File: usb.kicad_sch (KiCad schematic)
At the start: 4 parts, among them J3 USB_C_Receptacle_USB2.0_16P, U4 CP2102N-Axx-xQFN20, U5 USBLC6-2SC6

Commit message: did power and usb
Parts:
- added R10, R8, R9: 10k, symbol Device:R
- added R11, R12: 5.1k, Resistor_SMD:R_0402_1005Metric, symbol Device:R
- added R7: 4.7k, symbol Device:R
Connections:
- net SUSPb: now reaches U4.11 (~{SUSPEND})
- net SUSPb: now also R10.2
- net GND: now reaches U4.12 (GND), U4.21 (GND), U4.3 (GND)
- net GND: now also J3.A1 (GND), J3.A12 (GND), J3.B1 (GND), J3.B12 (GND), J3.S1 (SHIELD), U5.2 (GND), R10.1, R11.2, R12.2, R8.1, R9.1
- net SUSP: now reaches U4.14 (SUSPEND)
- net SUSP: now also R9.2
- net CTS: now reaches U4.15 (~{CTS})
- net RTS: now reaches U4.16 (~{RTS})
- net RXD: now reaches U4.17 (RXD)
- net TXD: now reaches U4.18 (TXD)
- net TXD: now also R8.2
- net D+: now reaches U4.4 (D+)
- net D+: now also J3.A6 (D+), J3.B6 (D+), U5.3 (I/O2), U5.4 (I/O2)
- net D-: now reaches U4.5 (D-)
- net D-: now also J3.A7 (D-), J3.B7 (D-), U5.1 (I/O1), U5.6 (I/O1)
- net +5V: now reaches U4.8 (VBUS)
- net +5V: now also F2.1, U5.5 (VBUS)
- net RSTb: now reaches U4.9 (~{RST})
- net RSTb: now also R7.2
- net at F2.2: now also J3.A4 (VBUS), J3.A9 (VBUS), J3.B4 (VBUS), J3.B9 (VBUS)
- net CC2: now reaches J3.A5 (CC1)
- net CC2: now also R12.1
- net CC1: now reaches J3.B5 (CC2)
- net CC1: now also R11.1
- new net +3.3V: R7.1
- no-connect marks 0 -> 9
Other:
- note added: "for break signaling"
- moved on the sheet: F2

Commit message: changed the switch converter to a LDOs
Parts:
- U4: footprint Package_DFN_QFN:SiliconLabs_QFN-20-1EP_3x3mm_P0.5mm -> Package_DFN_QFN:SiliconLabs_QFN-20-1EP_3x3mm_P0.5mm_EP1.8x1.8mm
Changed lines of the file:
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@@
 			)
 		)
-		(property "Footprint" "Package_DFN_QFN:SiliconLabs_QFN-20-1EP_3x3mm_P0.5mm"
+		(property "Footprint" "Package_DFN_QFN:SiliconLabs_QFN-20-1EP_3x3mm_P0.5mm_EP1.8x1.8mm"
 			(at 232.41 113.03 0)
 			(effects

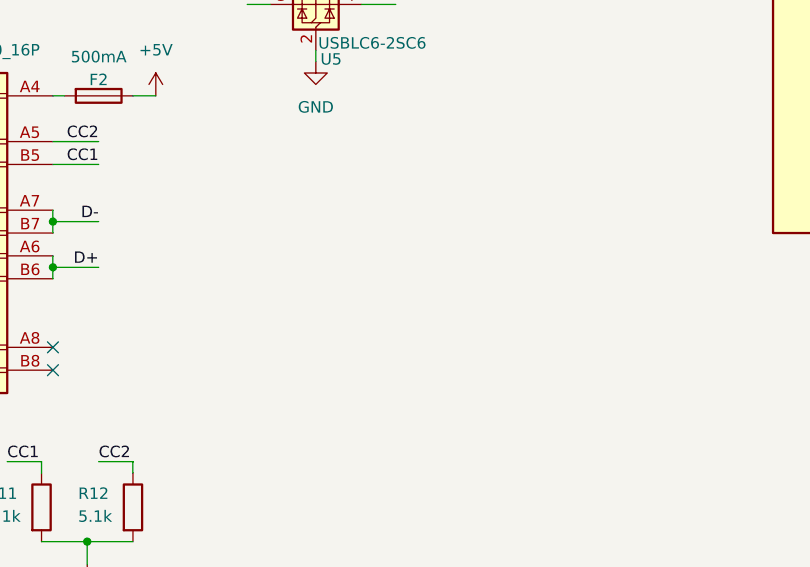
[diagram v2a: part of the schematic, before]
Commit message: re-did power with the new small LDOs and power system
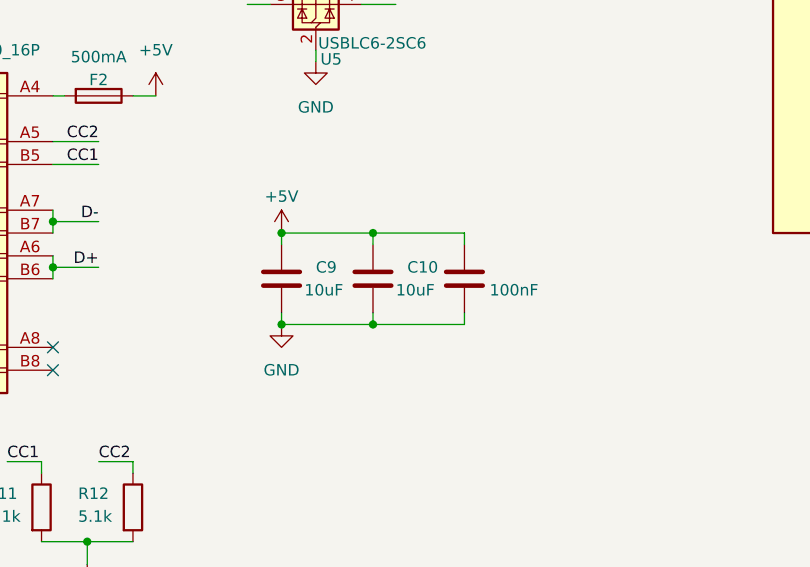
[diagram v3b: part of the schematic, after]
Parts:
- added C10, C9: 10uF, symbol Device:C
- added C11: 100nF, symbol Device:C
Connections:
- net +5V: now also C10.1, C11.1, C9.1
- net GND: now also C10.2, C11.2, C9.2

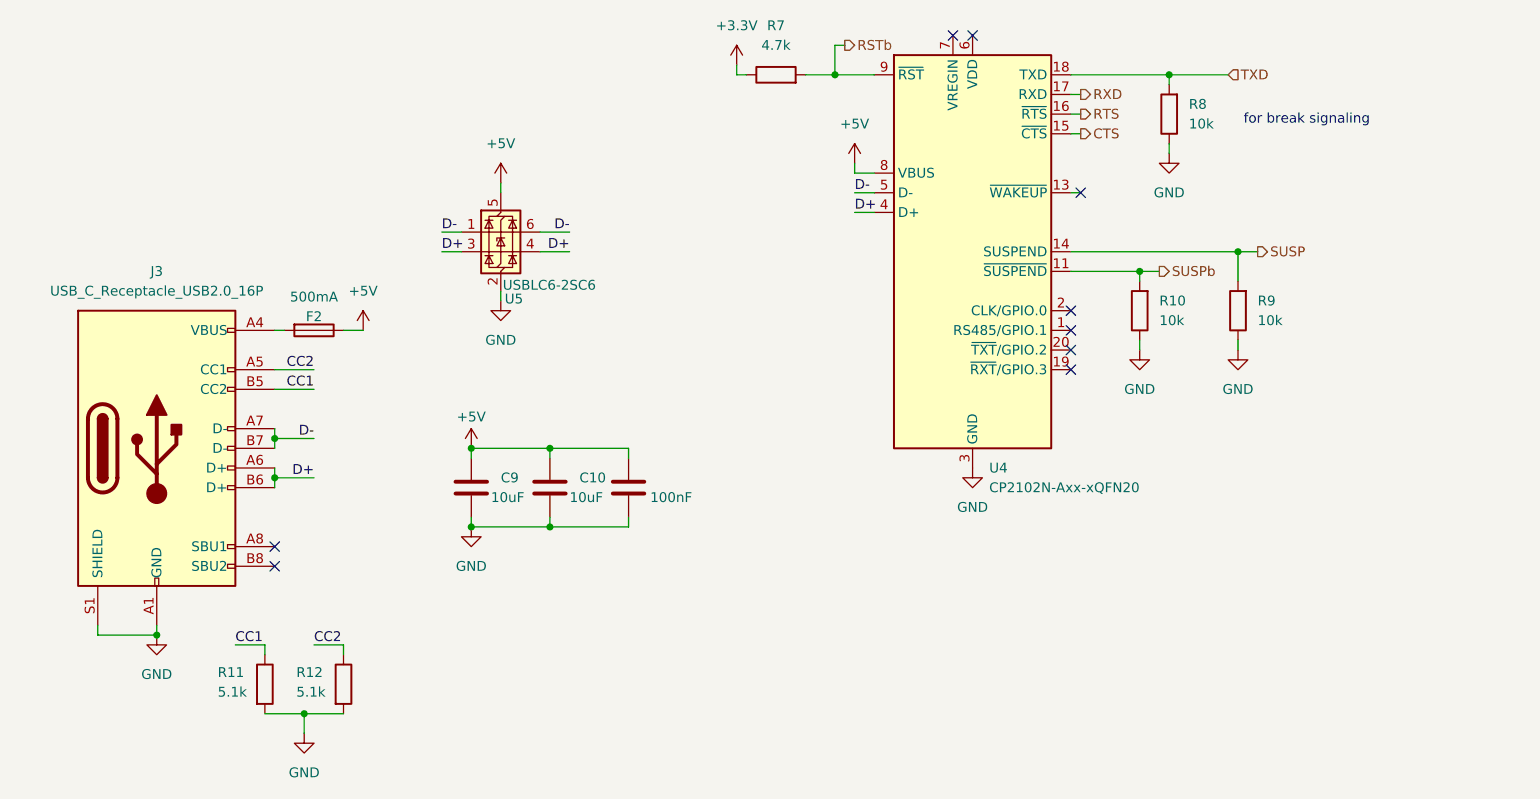
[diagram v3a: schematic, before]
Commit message: i2c, i2s, uart, en, sd card
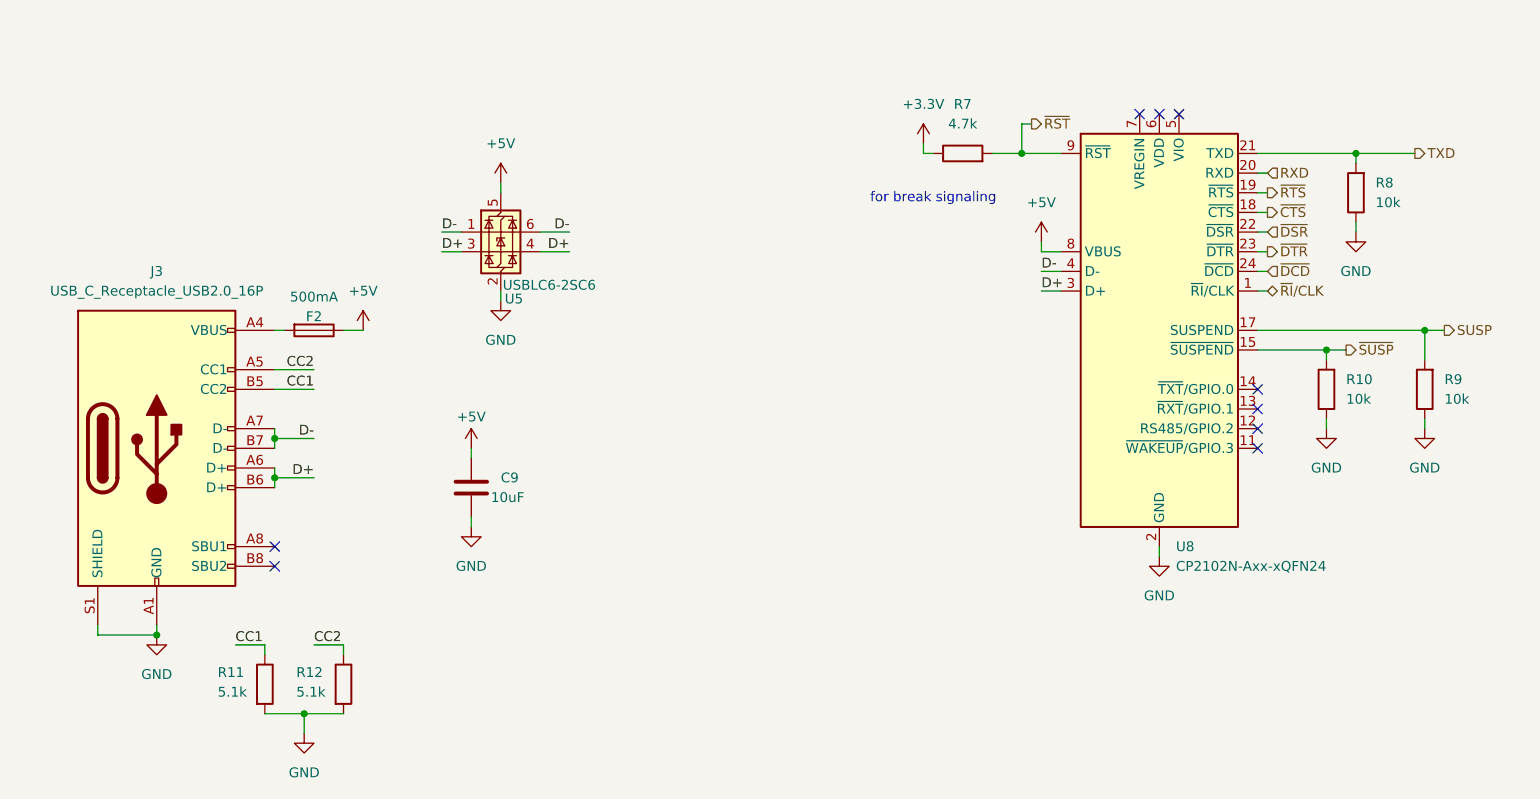
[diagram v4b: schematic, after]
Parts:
- removed C10: 10uF, symbol Device:C
- removed C11: 100nF, symbol Device:C
- removed U4: CP2102N-Axx-xQFN20, Package_DFN_QFN:SiliconLabs_QFN-20-1EP_3x3mm_P0.5mm_EP1.8x1.8mm, symbol Interface_USB:CP2102N-Axx-xQFN20
- added U8: CP2102N-Axx-xQFN24, Package_DFN_QFN:QFN-24-1EP_4x4mm_P0.5mm_EP2.6x2.6mm, symbol Interface_USB:CP2102N-Axx-xQFN24
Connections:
- net +5V: now also U8.8 (VBUS)
- net D+: now also U8.3 (D+)
- net D-: now also U8.4 (D-)
- net GND: now also U8.2 (GND), U8.25 (GND)
- net RXD: now also U8.20 (RXD)
- net SUSP: now also U8.17 (SUSPEND)
- net TXD: now also U8.21 (TXD)
- net RSTb renamed ~{RST}
- net ~{RST}: now also U8.9 (~{RST})
- net SUSPb renamed ~{SUSP}
- net ~{SUSP}: now also U8.15 (~{SUSPEND})
- new net ~{CTS}: U8.18 (~{CTS})
- new net ~{DCD}: U8.24 (~{DCD})
- new net ~{DSR}: U8.22 (~{DSR})
- new net ~{DTR}: U8.23 (~{DTR})
- new net ~{RI}/CLK: U8.1 (~{RI}/CLK)
- new net ~{RTS}: U8.19 (~{RTS})
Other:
- moved on the sheet: R10, R7, R8, R9

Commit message: esd, jack, io expander, led, power swquence
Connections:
- net GND: no longer J3.S1 (SHIELD)
- no-connect marks 9 -> 10
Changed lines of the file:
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@@
-	)
-	(junction
-		(at 95.25 135.89)
-		(diameter 0)
-		(color 0 0 0 0)
 	)
 	(junction
@@
 	)
 	(no_connect
+		(at 87.63 134.62)
+	)
+	(no_connect
 		(at 237.49 109.22)
 	)
@@
 	(wire
 		(pts
-			(xy 87.63 135.89) (xy 95.25 135.89)
-		)
-		(stroke
-			(width 0)
-			(type default)
-		)
-	)
-	(wire
-		(pts
 			(xy 250.19 83.82) (xy 250.19 82.55)
 		)
@@
 		)
 		(stroke
-			(width 0)
-			(type default)
-		)
-	)
-	(wire
-		(pts
-			(xy 87.63 135.89) (xy 87.63 134.62)
-		)
-		(stroke

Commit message: segmented schematci
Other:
- note added: "ESD"
- note added: "USB PORT"
- note added: "USB to UART"
- moved on the sheet: C9, R11, R12, U5
